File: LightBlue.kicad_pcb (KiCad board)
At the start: 4 copper layers, 120 x 120.1 mm, 300 parts, among them J1 Barrel_Jack, J10 Conn_02x04_Odd_Even, J11 Conn_02x05_Odd_Even, J12 Bus_M.2_Socket_M, J13 Conn_01x03_Male, J2 RJ45_LINK-PP_LPJG0926HENL_Hor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, J3 USB_C_Receptacle_USB2.0, J4 USB_A_Stacked, J5 AudioJack, J6 HDMI_D_2.0, J7 Micro_SD_Card_Det, J8 SiLabs Mini Debug, J9 Conn_Coaxial, M1 Fan_4pin, Q1 DMP3013SFV-7, Q2 BSZ440N10NS3GATMA1, SW1 SW_USER, SW2 SW_WIPE, T1 PA2467NL, U1 RaspberryPi-CM4Lite, U10 TPD4EUSB30, U11 SiliconLabs-MGM210P, U12 PCM5121PW, U13 TLV74033PDBVR, U14 TPD4EUSB30, U15 TPD4EUSB30, U16 BD9D321EFJ, U17 BD9D321EFJ, U18 74LVC1G07, U19 74LVC1G07, U2 DF40C-100DS-0.4V, U20 LP5569RTWR, U21 PCF85063AT, U22 RT9742GGJ5, U23 TPS23734, U24 TCMT1107, U3 DF40C-100DS-0.4V, U4 CP2102N-Axx-xQFN20, U5 FSUSB42MUX, U6 FSUSB42MUX, U7 USB2422, U8 TPD4EUSB30, U9 AP2191W, Y1 24MHz, Y2 X32K768S301

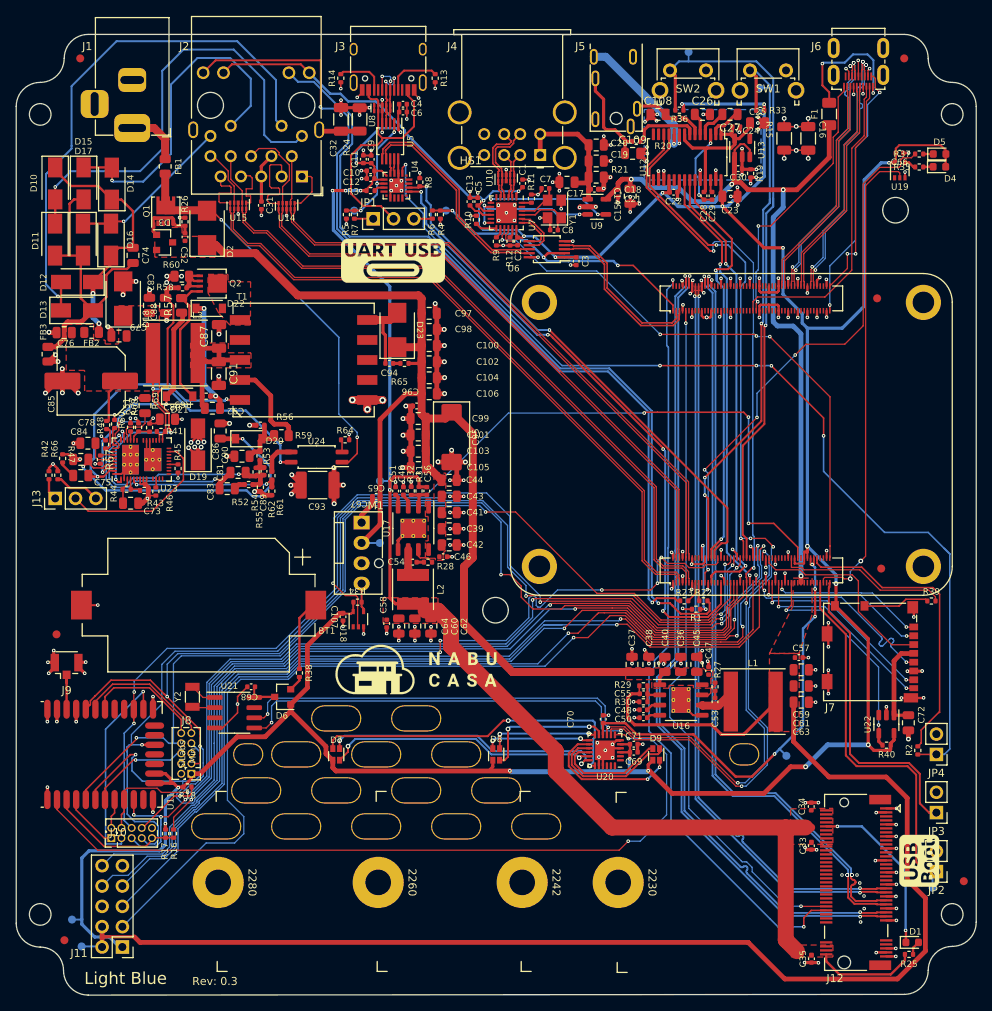
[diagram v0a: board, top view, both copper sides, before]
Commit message: Rotate jumpers by 90°
Rotate jumpers J2 through J4 by 90° degrees. This makes all jumper
orient the same and makes space for silk screen.

Signed-off-by: Stefan Agner <stefan@agner.ch>
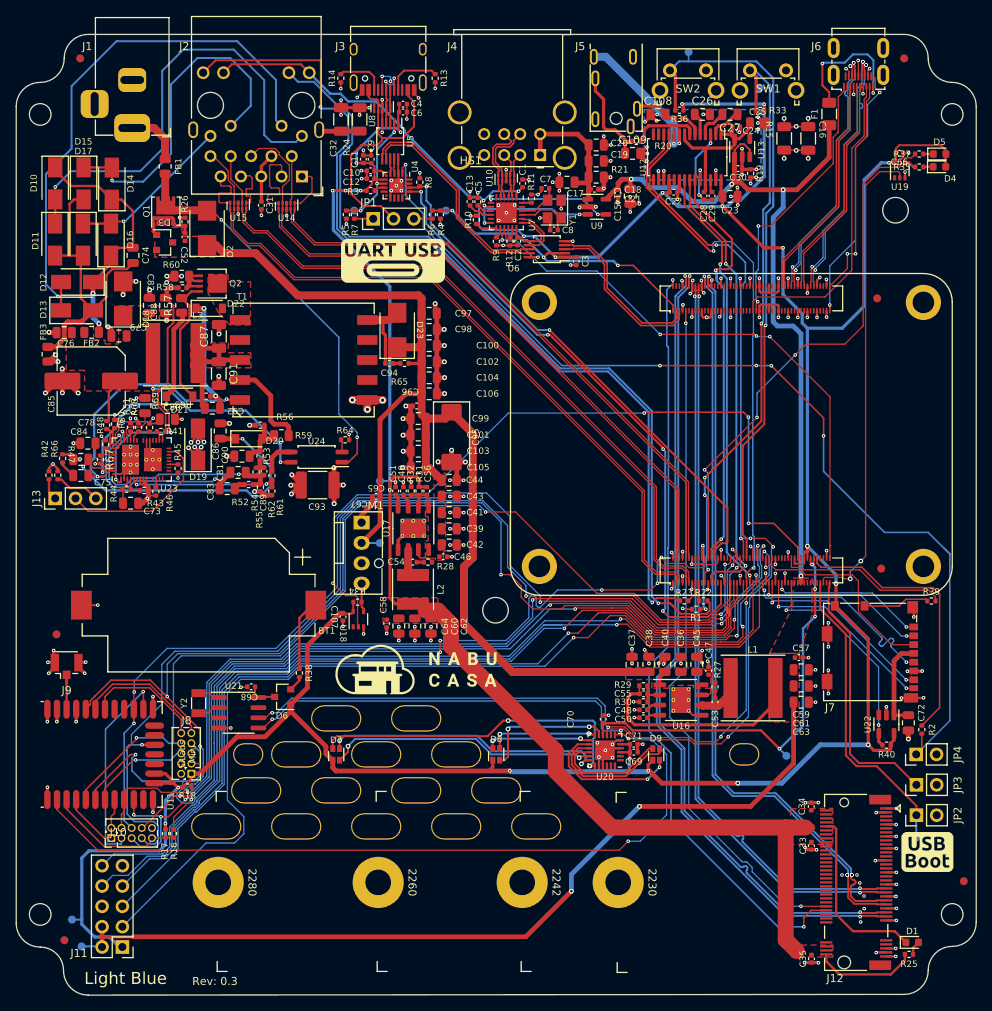
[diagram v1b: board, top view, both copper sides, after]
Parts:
- moved JP2 7.48 mm to (142.5, 127.6), turned to 90 degrees
- moved TP1 6.60 mm to (142.5, 130.4)
- moved JP3 4.28 mm to (142.5, 123.8), turned to 90 degrees
- moved R2 2.65 mm to (143.2, 116.9)
- moved JP4 2.53 mm to (142.5, 120.0), turned to 90 degrees
- moved L1 1.70 mm to (122.1, 111.7)
- moved Ref** 1.50 mm to (143.9, 132.2), turned to 0 degrees
- moved Y2 1.11 mm to (52.8, 113.6)
- moved U21 0.52 mm to (57.8, 114.8)
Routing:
- net +5V: track 280.5 -> 235.3 mm, vias 4 -> 6
- net /SDA: track 171.0 -> 158.0 mm
- net /SCL: track 164.3 -> 151.6 mm
- net /CM4/~RPI_BOOT: track 48.9 -> 38.3 mm
- net /CM4/GLOBAL_EN: track 38.6 -> 32.5 mm
- net GND: track 308.1 -> 303.5 mm, vias 247 -> 248
- net /CM4/RUN_PG: track 37.8 -> 34.9 mm
- net +1V8: track 56.0 -> 53.2 mm
- net +3V3: track 462.4 -> 461.4 mm
- net Net-(D1-Pad1): track 21.2 -> 22.2 mm, vias 2 -> 0
- net /CM4/RESET_CM4: track 127.7 -> 128.7 mm
- net Net-(U21-Pad1): track 3.34 -> 2.75 mm

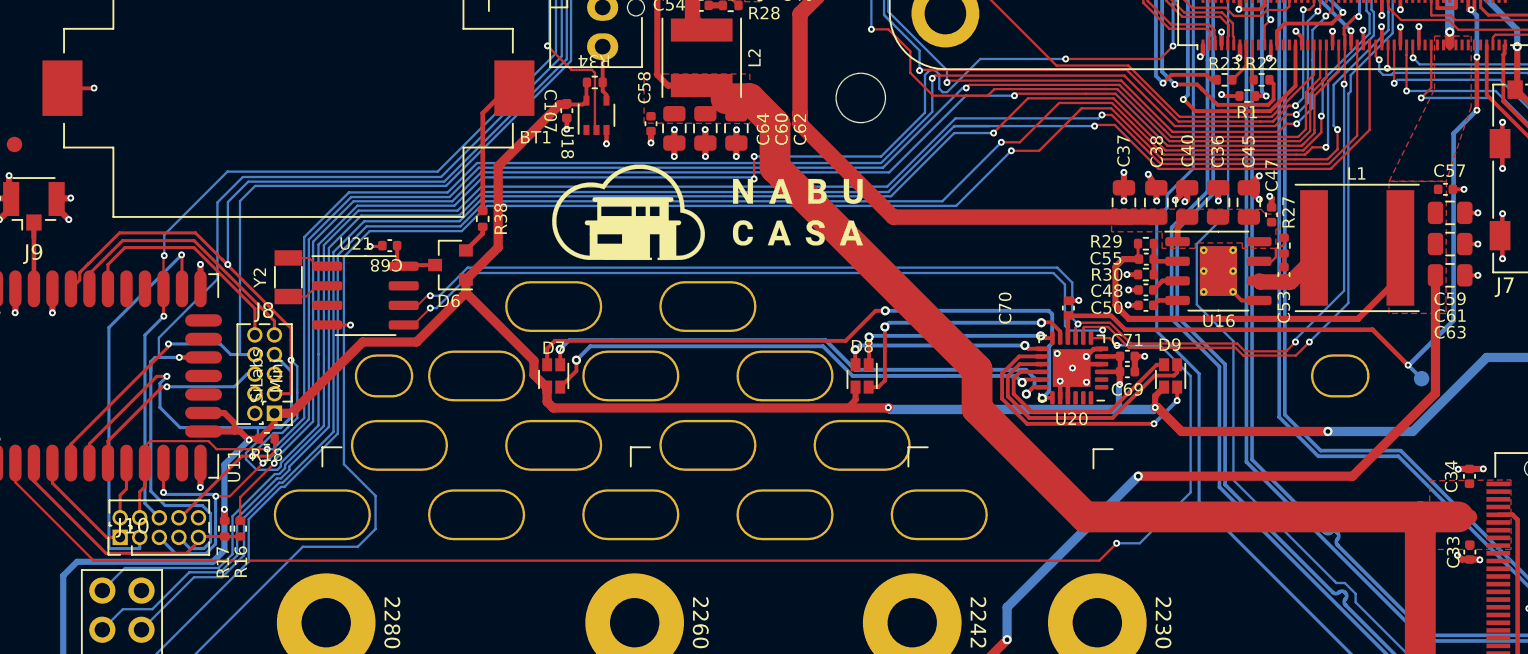
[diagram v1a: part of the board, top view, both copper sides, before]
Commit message: Move LP5569RTWR LED controller away from light diffuser
Move the LP5569RTWR LED controller so it doesn't interfere with the
LED light diffuser if we decide to make it sit directly on the PCB.

Signed-off-by: Stefan Agner <stefan@agner.ch>
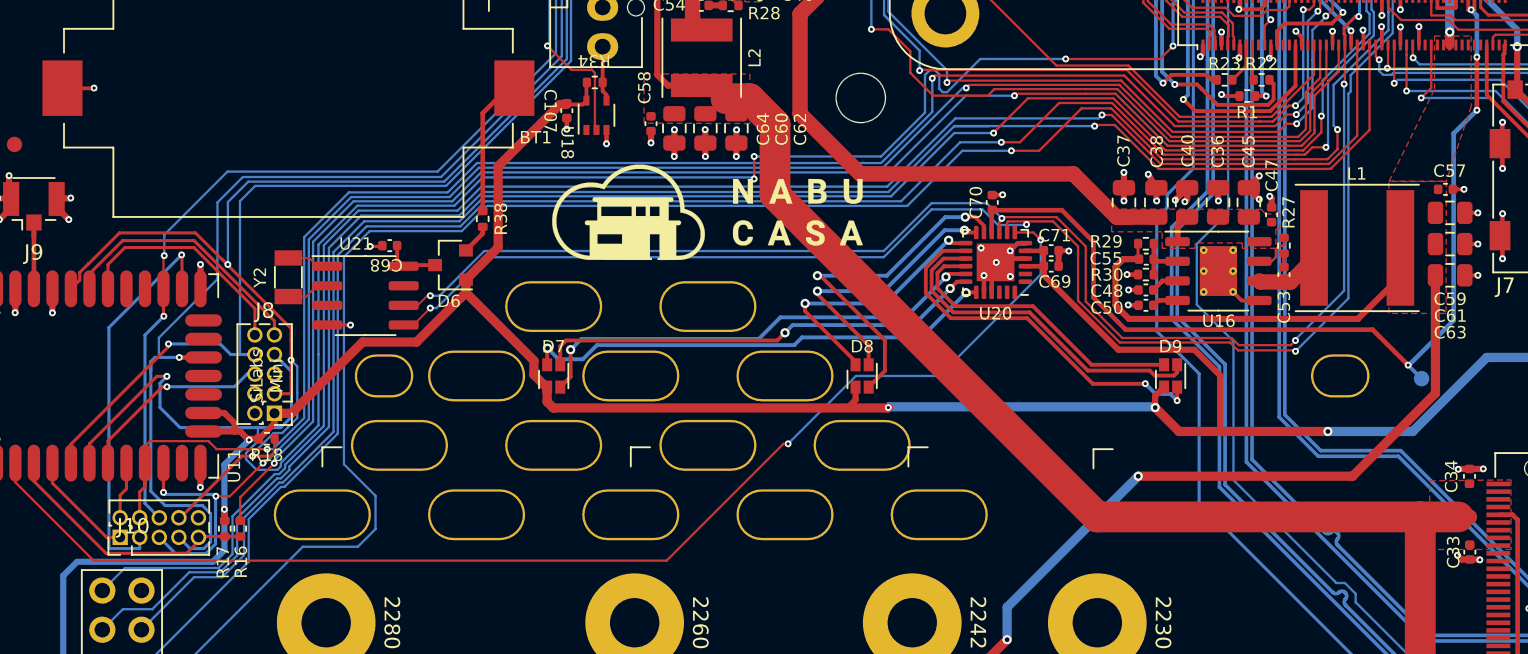
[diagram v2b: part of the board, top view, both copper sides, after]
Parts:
- moved C69 8.44 mm to (102.3, 112.9)
- moved C70 8.44 mm to (98.4, 108.8)
- moved C71 8.44 mm to (102.3, 111.9)
- moved U20 8.44 mm to (98.7, 112.6)
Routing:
- net /802.15.4 Radio/~LED_RADIO: track 96.4 -> 81.6 mm
- net Net-(D7-Pad1): track 41.3 -> 31.0 mm
- net +1V8: track 53.2 -> 63.1 mm
- net Net-(D9-Pad3): track 18.2 -> 24.8 mm
- net Net-(D7-Pad2): track 35.5 -> 29.2 mm
- net Net-(D8-Pad3): track 16.9 -> 22.6 mm
- net Net-(D9-Pad2): track 17.2 -> 22.7 mm
- net Net-(D9-Pad1): track 14.5 -> 19.8 mm
- net Net-(D8-Pad2): track 13.8 -> 18.1 mm
- net Net-(D8-Pad1): track 13.3 -> 17.5 mm
- net /SCL: track 151.6 -> 155.4 mm
- net /SDA: track 158.0 -> 161.5 mm
- net Net-(D7-Pad3): track 33.8 -> 30.4 mm
- net +3V3: track 461.4 -> 460.1 mm, vias 19 -> 18

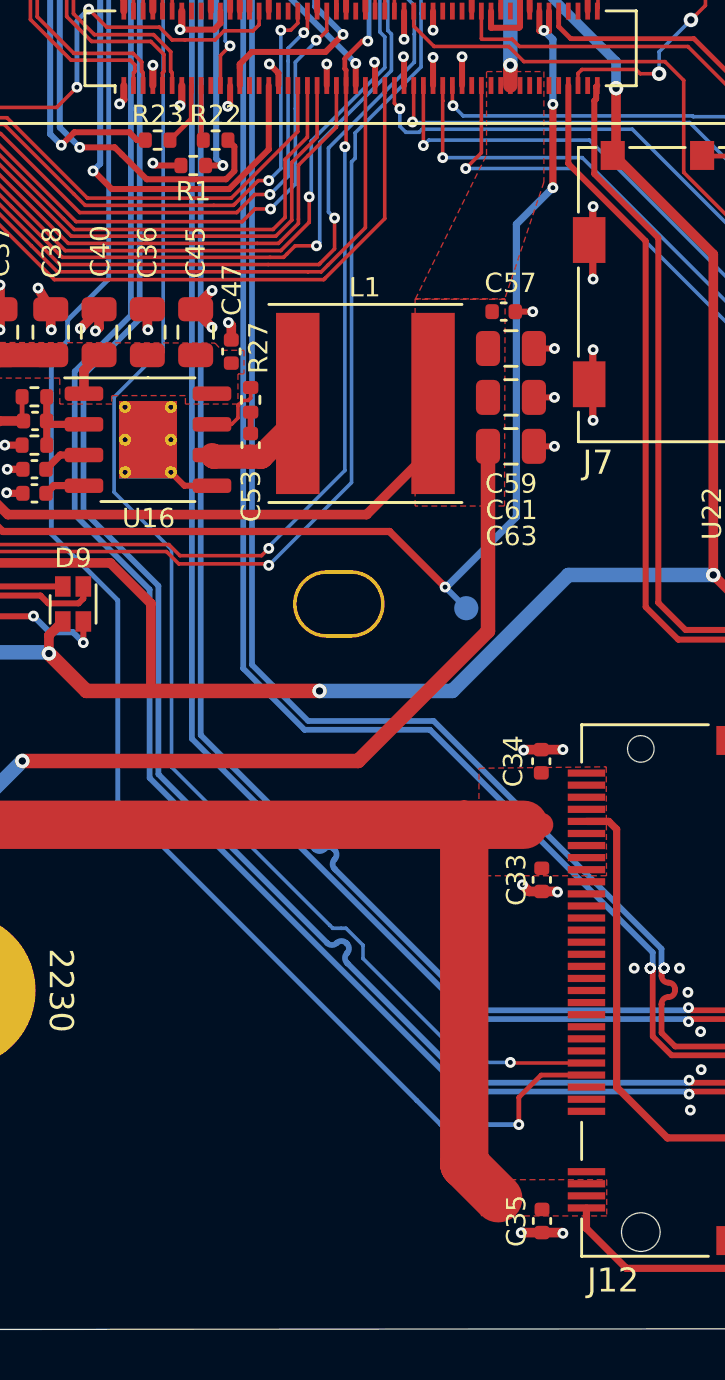
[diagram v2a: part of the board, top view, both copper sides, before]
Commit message: Add test points for I2C
Signed-off-by: Stefan Agner <stefan@agner.ch>
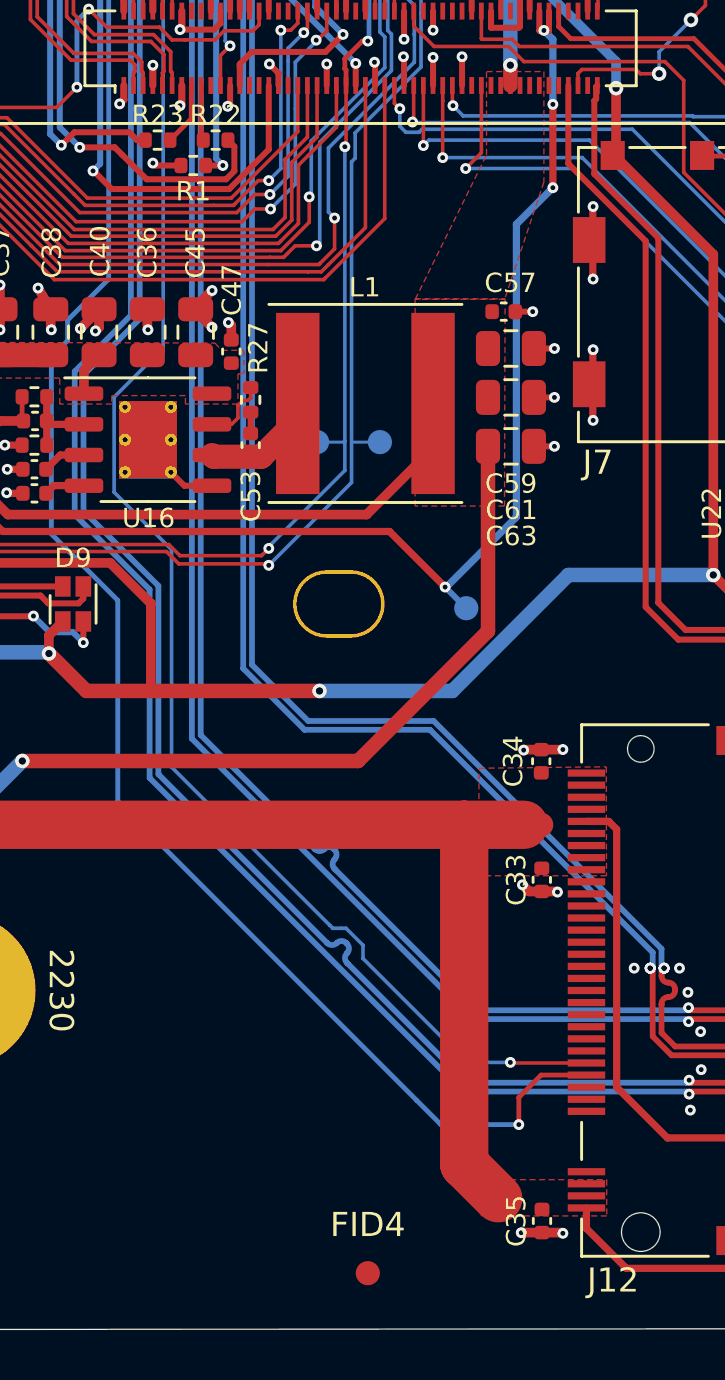
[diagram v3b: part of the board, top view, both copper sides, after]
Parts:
- added FID4: Fiducial, Fiducial:Fiducial_1mm_Mask2mm, F.Cu at (122.2, 147.7)
- added TP11: TestPoint, TestPoint:TestPoint_Pad_D1.0mm, B.Cu at (120.1, 113.3)
- added TP12: TestPoint, TestPoint:TestPoint_Pad_D1.0mm, B.Cu at (122.7, 113.3)
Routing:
- net /SDA: track 161.5 -> 162.7 mm
- net /SCL: track 155.4 -> 156.6 mm
